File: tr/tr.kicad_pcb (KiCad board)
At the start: 4 copper layers, 70 parts, among them J1 SMA, J2 SMA, J3 SMA, K1 CONN_3, Q3 STD2NK90ZT4, Q4 STD2NK90ZT4, U1 L6388E, U2 LT1631

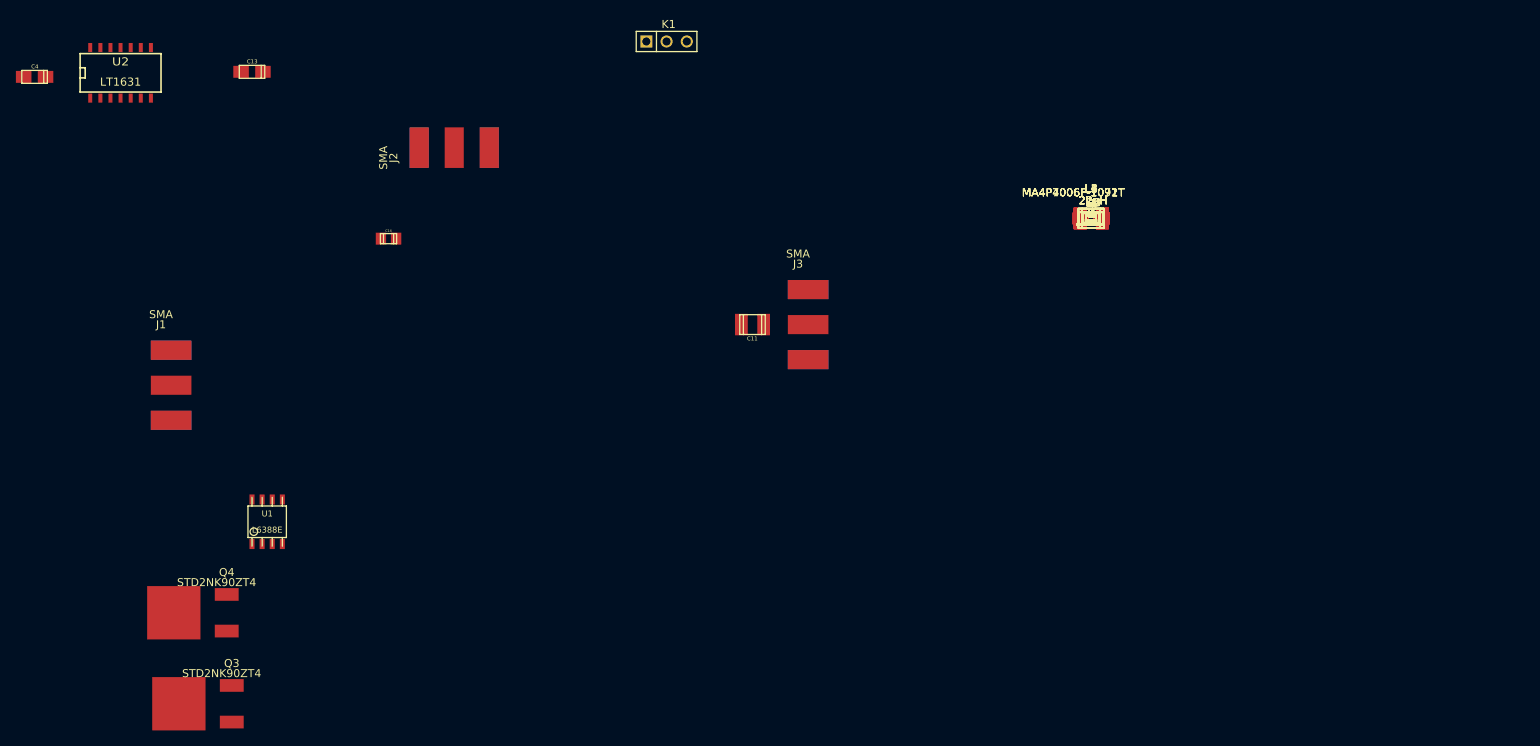
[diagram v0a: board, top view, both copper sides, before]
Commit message: component placement on tr
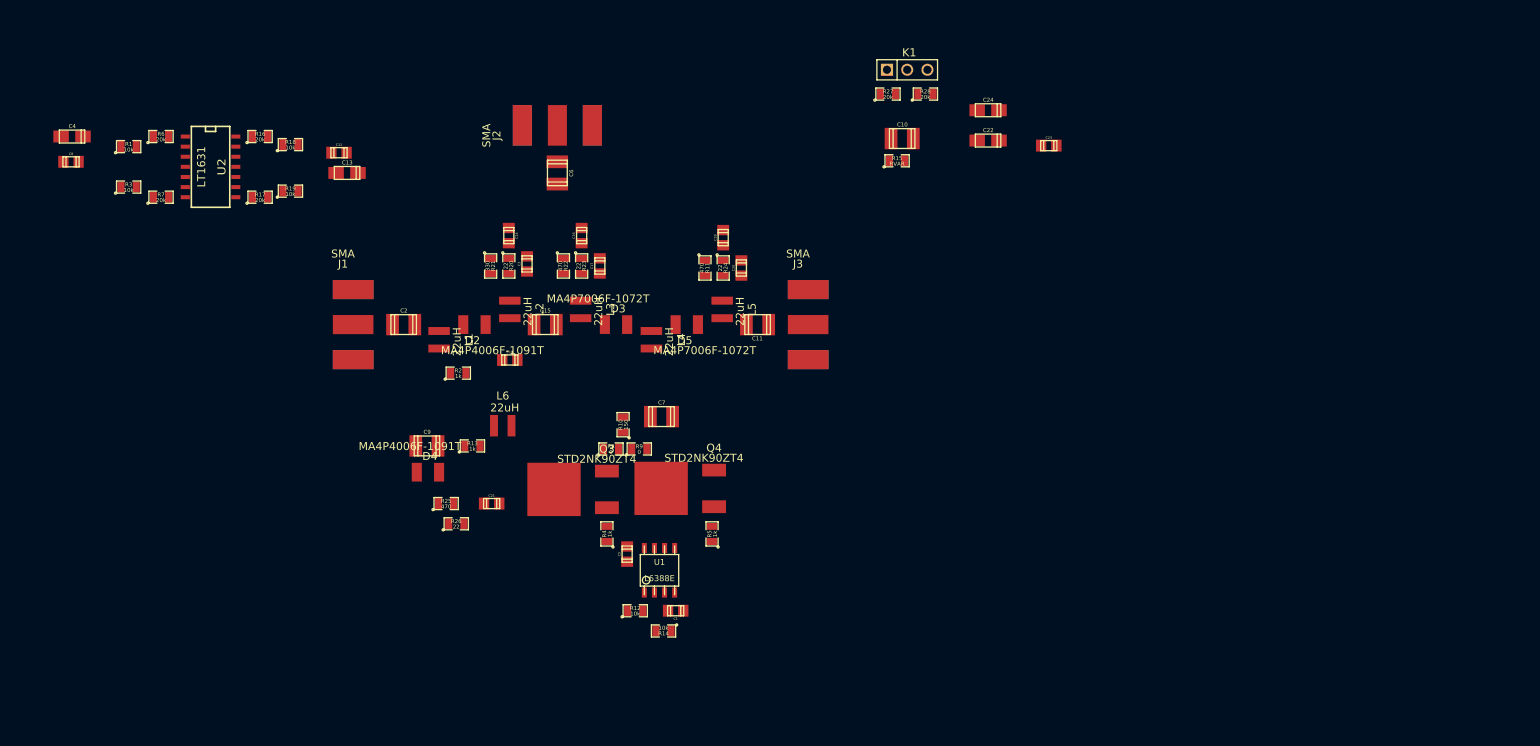
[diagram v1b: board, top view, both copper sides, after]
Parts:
- moved C8 128.3 mm to (29.3, 36.7)
- moved R1 121.2 mm to (36.6, 34.8)
- moved R3 121.0 mm to (36.6, 39.9)
- moved R6 117.3 mm to (40.6, 33.5)
- moved R7 116.9 mm to (40.6, 41.1)
- moved R16 104.9 mm to (53.1, 33.5)
- moved R17 104.4 mm to (53.1, 41.1)
- moved R18 101.0 mm to (56.9, 34.5)
- moved R19 100.6 mm to (56.9, 40.4)
- moved C12 94.8 mm to (63.0, 35.6)
- moved D4 89.2 mm to (74.2, 75.7)
- moved R25 88.6 mm to (76.5, 79.6)
- moved R26 88.5 mm to (77.7, 82.2)
- moved C9 88.2 mm to (74.0, 72.4)
- moved C2 87.4 mm to (71.1, 57.1)
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
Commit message: updated transmitter layout
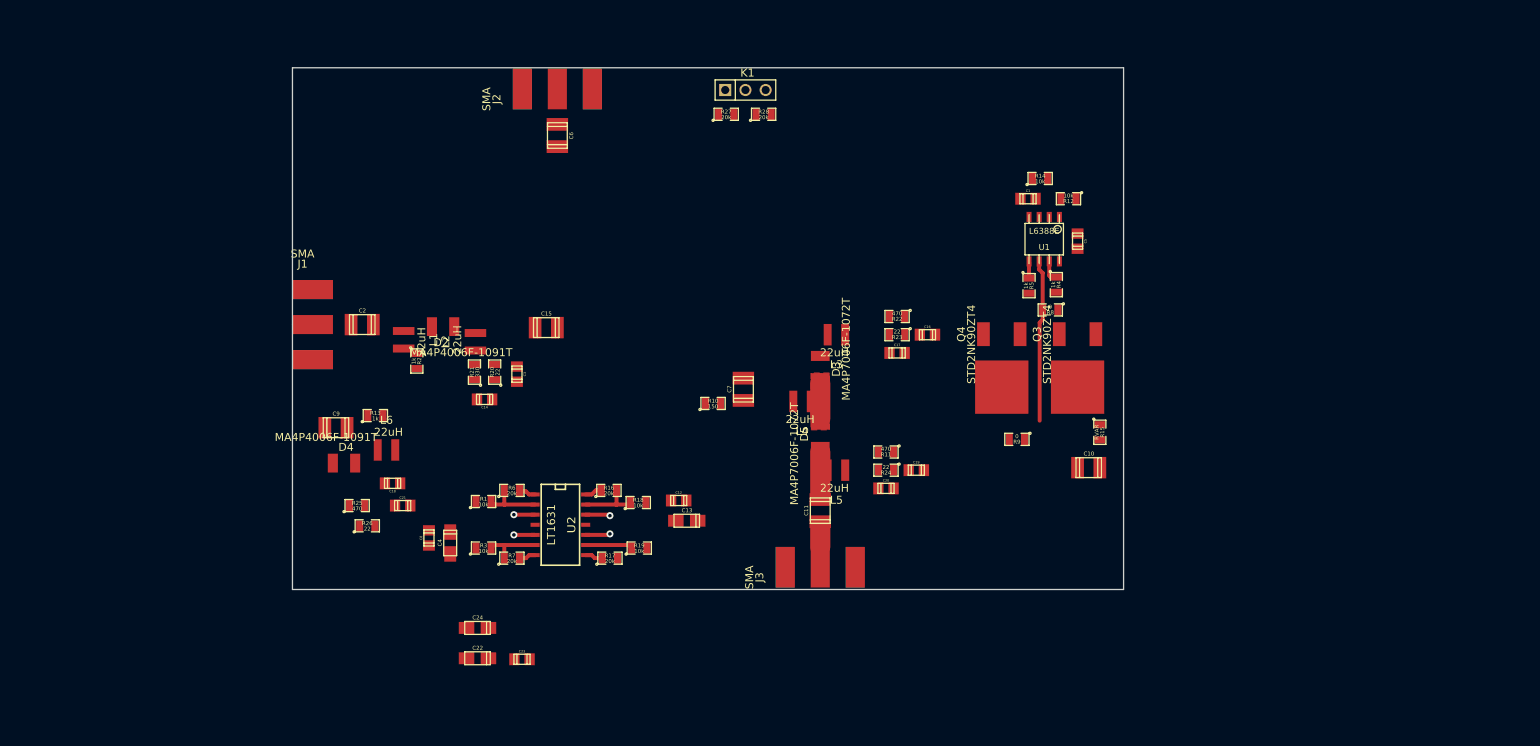
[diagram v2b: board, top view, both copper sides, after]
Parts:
- moved C23 92.4 mm to (86.0, 99.2)
- moved C22 91.3 mm to (80.4, 99.1)
- moved C24 91.3 mm to (80.4, 95.2)
- moved R12 75.1 mm to (154.6, 41.3), turned to 180 degrees
- moved R14 73.9 mm to (151.1, 38.8), turned to 0 degrees
- moved C4 69.7 mm to (77.0, 84.6), turned to 90 degrees
- moved C5 68.9 mm to (155.8, 46.7), turned to 270 degrees
- moved C1 68.1 mm to (149.5, 41.3), turned to 0 degrees
- moved C8 65.2 mm to (74.3, 83.9), turned to 90 degrees
- moved R4 64.6 mm to (153.1, 52.1), turned to 270 degrees
- moved U1 63.8 mm to (151.6, 46.4), turned to 180 degrees
- moved R3 63.6 mm to (81.2, 85.2)
- moved R7 63.2 mm to (84.7, 86.5)
- moved R17 63.1 mm to (97.0, 86.5)
- moved R1 63.0 mm to (81.2, 79.4)
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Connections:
- C5 pad 2: N-0000039 (its old number) -> /hvout
- C7 pad 2: N-0000048 (its old number) -> /hvbias
- C9 pad 2: N-0000034 (its old number) -> /hvdiode
- D3 pad 2: N-0000034 (its old number) -> /hvdiode
- D5 pad 2: N-0000034 (its old number) -> /hvdiode
- L4 pad 1: N-0000034 (its old number) -> /hvdiode
- L4 pad 2: N-0000048 (its old number) -> /hvbias
- Q3 pad S: N-0000028 (its old number) -> /hvs
- Q4 pad D: N-0000029 (its old number) -> /hvd
- R10 pad 1: N-0000039 (its old number) -> /hvout
- R10 pad 2: N-0000048 (its old number) -> /hvbias
- R8 pad 1: N-0000028 (its old number) -> /hvs
- R8 pad 2: N-0000039 (its old number) -> /hvout
- R9 pad 1: N-0000039 (its old number) -> /hvout
- R9 pad 2: N-0000029 (its old number) -> /hvd
- U1 pad 6: N-0000039 (its old number) -> /hvout
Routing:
- net /hvout: track 0.00 -> 20.3 mm
- net GND: track 0.00 -> 12.2 mm, vias 0 -> 4
- net N-0000037: track 0.00 -> 9.91 mm
- net /hvdiode: track 0.00 -> 9.25 mm
- net N-000005: track 0.00 -> 7.60 mm
- net N-0000015: track 0.00 -> 7.52 mm
- net N-0000010: track 0.00 -> 7.40 mm
- net N-000001: track 0.00 -> 5.94 mm
- net N-0000029: track 0.00 -> 5.71 mm
- net N-0000039: track 0.00 -> 2.75 mm
- net N-000003: track 0.00 -> 2.25 mm
- net /OUTD: track 0.00 -> 2.18 mm
- net /OUTA: track 0.00 -> 2.18 mm
- net N-000002: track 0.00 -> 2.13 mm
- net N-0000038: track 0.00 -> 2.10 mm
- added copper zone on Inner1.Cu, net GND
- added copper zone on F.Cu, net N-0000034
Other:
- board outline added: 104.4 x 65.5 mm
- net class 50ohm_1to3 added: clearance 0.254, trace_width 2.8, via_dia 0.889, via_drill 0.635
- net class hv added: clearance 2, trace_width 0.254, via_dia 0.889, via_drill 0.635

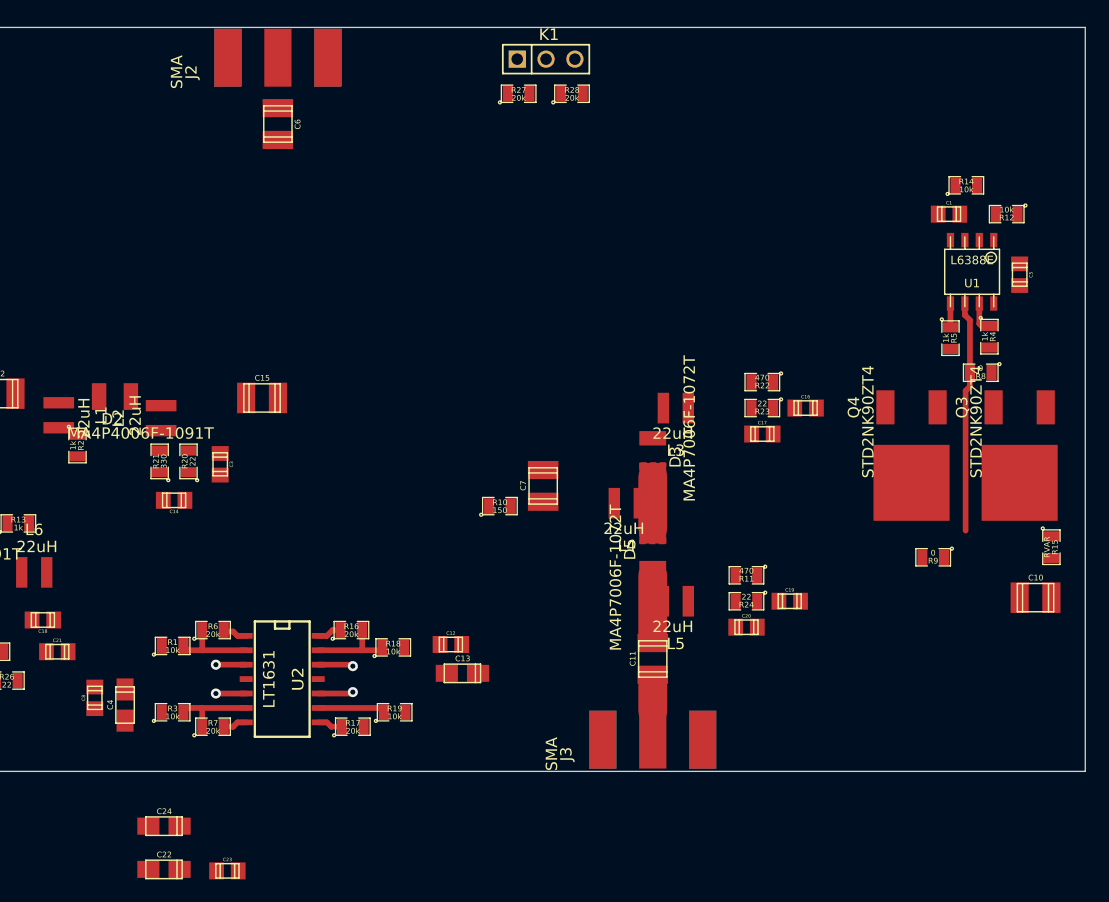
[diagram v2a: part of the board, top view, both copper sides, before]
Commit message: component placement on hv power supply
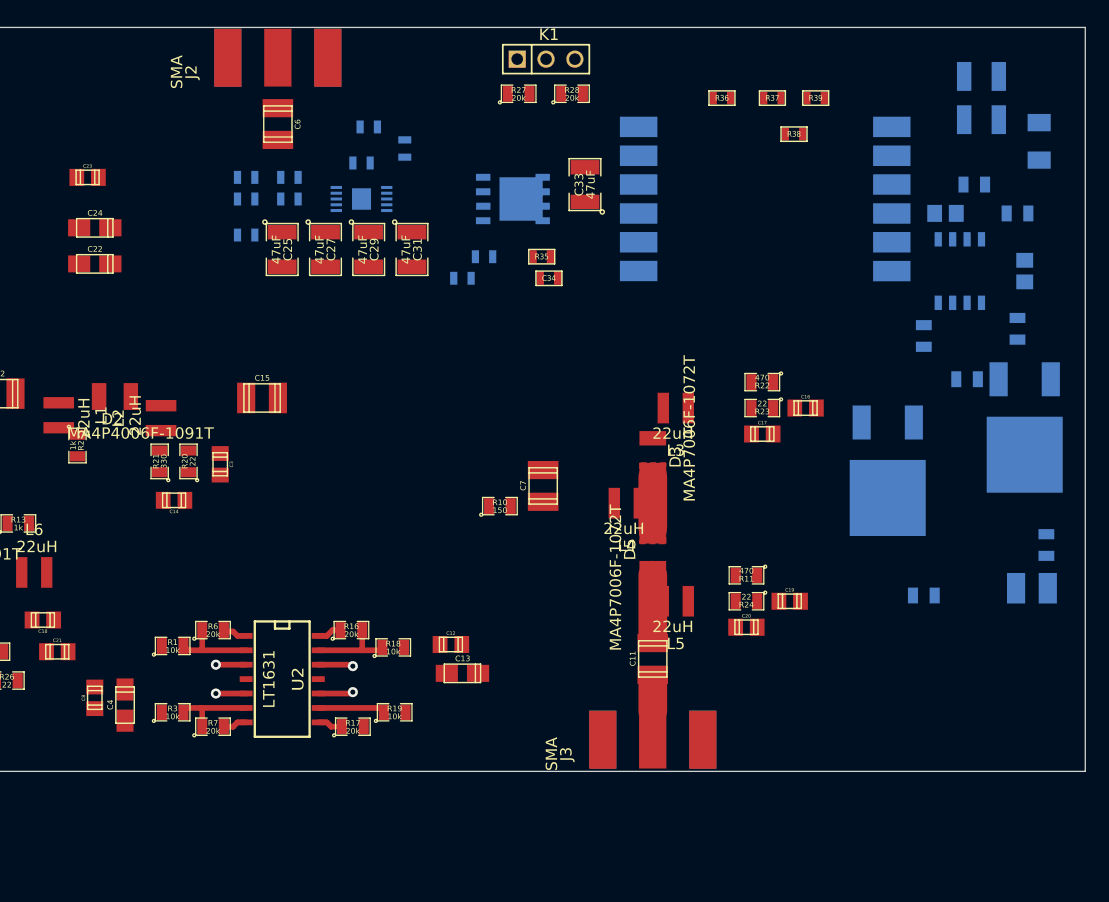
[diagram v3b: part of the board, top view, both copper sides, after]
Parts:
- added C25: 47uF, SM1210, F.Cu at (90.8, 44.5)
- added C26: 100pF, SM0603, B.Cu at (87.6, 43.2)
- added C27: 47uF, SM1210, F.Cu at (94.6, 44.5)
- added C28: 22nF, SM0603, B.Cu at (87.6, 40.0)
- added C29: 47uF, SM1210, F.Cu at (98.4, 44.5)
- added C30: 100nF, SM0603, B.Cu at (91.4, 38.1)
- added C31: 47uF, SM1210, F.Cu at (102.2, 44.5)
- added C32: 10nF, SM0603, B.Cu at (98.4, 33.7)
- added C33: 47uF, SM1210, F.Cu at (117.5, 38.7)
- added C34: 220pF, SM0603, F.Cu at (114.3, 47.0)
- added C35: 68nF, SM1210, B.Cu at (152.4, 33.0)
- added C36: 68nF, SM1210, B.Cu at (152.4, 29.2)
- added Q1: Si7850, SO8PowerPAK, B.Cu at (111.1, 40.0)
- added R29: 6.8k, SM0603, B.Cu at (87.6, 38.1)
- added R30: 140k, SM0603, B.Cu at (91.4, 40.0)
- added R31: 46.4k, SM0603, B.Cu at (97.8, 36.8)
- added R32: 105k, SM0603, B.Cu at (101.6, 35.6)
- added R33: 22, SM0603, B.Cu at (106.7, 47.0)
- added R34: .02, SM0603, B.Cu at (108.6, 45.1)
- added R35: 22, SM0603, F.Cu at (113.7, 45.1)
- added R36: 1.5M, SM0603, F.Cu at (129.5, 31.1)
- added R37: 1M, SM0603, F.Cu at (134.0, 31.1)
- added R38: 1M, SM0603, F.Cu at (135.9, 34.3)
- added R39: 16.2k, SM0603, F.Cu at (137.8, 31.1)
- added R40: 1M, SM1206, B.Cu at (157.5, 34.9)
- added T1: DA2033-AL_, DA2033-AL, B.Cu at (133.3, 40.0)
- added U3: LT3757, MSOP10EP-0.5, B.Cu at (97.8, 40.0)
- C1, C10, C5, Q3, Q4, R12, R14, R15, R4, R5, R8, R9, U1: moved to B.Cu
- moved C23 62.3 mm to (73.7, 38.1)
- moved C22 53.7 mm to (74.3, 45.7)
- moved C24 53.1 mm to (74.3, 42.5)
- moved R9 3.47 mm to (147.3, 74.9)
- moved R4 2.57 mm to (155.6, 51.4)
- moved Q3 2.52 mm to (156.2, 55.9)
- moved Q4 2.48 mm to (144.1, 59.7)
- moved R5 2.36 mm to (147.3, 52.1), turned to 90 degrees
- moved R8 1.34 mm to (151.1, 55.9)
- moved U1 1.08 mm to (150.5, 46.4), turned to 0 degrees
- moved R12 0.95 mm to (155.6, 41.3)
- moved C10 0.88 mm to (156.8, 74.3)
- moved R14 0.70 mm to (151.8, 38.7)
- moved C5 0.55 mm to (156.2, 46.4), turned to 90 degrees
- moved R15 0.48 mm to (158.1, 70.5), turned to 90 degrees
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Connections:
- R15 pad 2: (no net) -> N-0000033
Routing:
- net /hvout: track 20.3 -> 0.00 mm
- net N-0000057: track 2.75 -> 0.00 mm
- net N-0000029: track 2.10 -> 0.00 mm
- added copper zone on F.Cu, net N-0000034
- removed copper zone on F.Cu, net N-0000024
